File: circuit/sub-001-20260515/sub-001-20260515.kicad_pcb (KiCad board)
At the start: 2 copper layers, 114.3 x 107 mm, 147 parts, among them J1 Conn_NeoPixel, J2 Conn_01x02_Socket, J3 Conn_Power, J4 Conn_Main, Q1 BSS138, Q2 BSS138, Q3 BSS138, Q4 BSS138, Q5 BSS138, Q6 BSS138, Q7 BSS138, Q8 BSS138, U11 LM1117GS-3.3, U12 NE555DR, U13 NE555DR, U14 LM1117GS-3.3, U15 LM1117GS-3.3, U18 NE555DR, U19 NE555DR, U2 LM1117GS-3.3, U20 TSSP58038, U21 TSSP58038, U22 NE555DR, U23 NE555DR, U24 TSSP58038, U25 TSSP58038, U26 HC-SR04, U27 HC-SR04, U28 HC-SR04, U29 HC-SR04, U4 NE555DR, U5 NE555DR, U7 LM1117GS-3.3, U9 LM1117MP-3.3

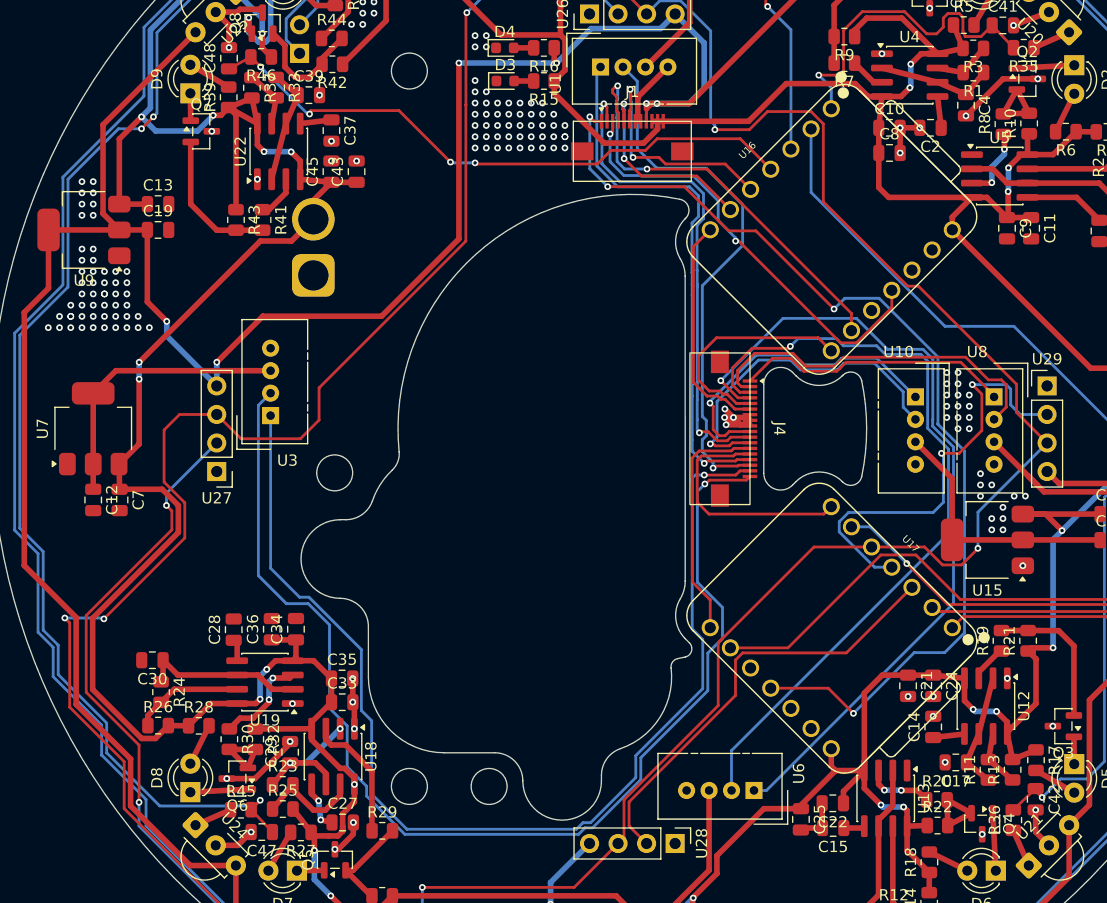
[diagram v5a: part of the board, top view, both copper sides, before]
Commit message: Update ラインセンサ基板の配線を進めた
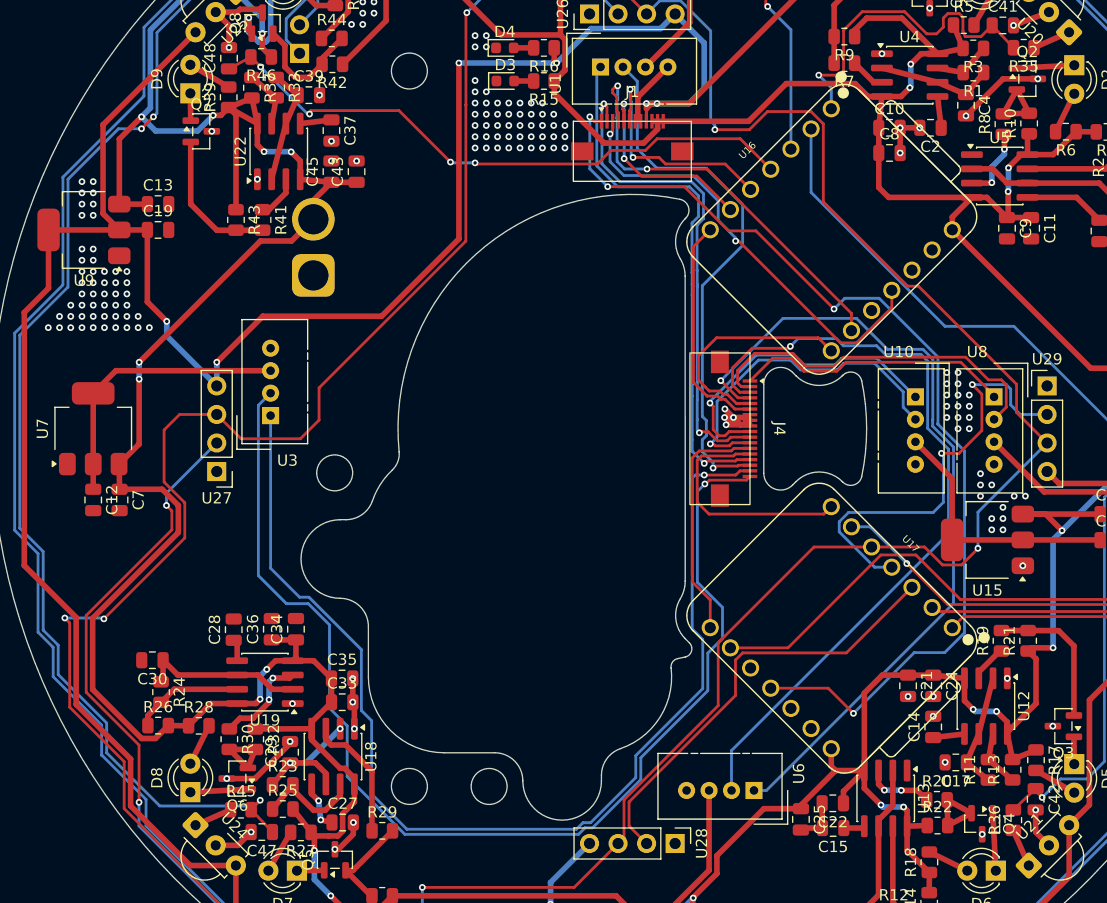
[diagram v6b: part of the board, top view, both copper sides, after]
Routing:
- net 3.3V-unitV4: track 28.3 -> 27.2 mm
- net +5V: track 553.9 -> 553.4 mm, vias 27 -> 26
- net GND: vias 178 -> 175
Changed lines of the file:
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@@
 	)
 	(segment
-		(start 36.04 5)
-		(end 35.285 4.245)
-		(width 0.5)
-		(layer "F.Cu")
-		(net "3.3V-unitV4")
-	)
-	(segment
 		(start 48 -5.39)
 		(end 48 -3.15)
@@
 	)
 	(via
-		(at -50 -10)
-		(size 0.6)
-		(drill 0.3)
-		(layers "F.Cu" "B.Cu")
-		(free yes)
-		(net "GND")
-	)
-	(via
 		(at -25 -36)
 		(size 0.6)
@@
 	)
 	(via
-		(at -6 -26)
-		(size 0.6)
-		(drill 0.3)
-		(layers "F.Cu" "B.Cu")
-		(free yes)
-		(net "GND")
-	)
-	(via
 		(at -48 -21)
 		(size 0.6)
@@
 	)
 	(via
-		(at -47 -12)
-		(size 0.6)
-		(drill 0.3)
-		(layers "F.Cu" "B.Cu")
-		(free yes)
-		(net "GND")
-	)
-	(via
 		(at -14 -31)
 		(size 0.6)
@@
 	)
 	(segment
-		(start 2.25 -26.675)
-		(end 2.25 -27.375)
-		(width 0.5)
-		(layer "F.Cu")
-		(net "+5V")
-	)
-	(segment
 		(start -25.612316 30.24)
 		(end -24.745 31.107316)
@@
 	)
 	(segment
-		(start -2.505 -25.43)
-		(end 1.005 -25.43)
-		(width 0.5)
-		(layer "F.Cu")
-		(net "+5V")
-	)
-	(segment
 		(start 33.36 -18.8)
 		(end 35.51 -18.8)
@@
 	)
 	(segment
+		(start -6.9575 -29.8825)
+		(end -2.505 -25.43)
+		(width 0.5)
+		(layer "F.Cu")
+		(net "+5V")
+	)
+	(segment
+		(start -6.9575 -30.96)
+		(end -6.9575 -29.8825)
+		(width 0.5)
+		(layer "F.Cu")
+		(net "+5V")
+	)
+	(segment
 		(start -27.6725 -34.75)
 		(end -27.668122 -34.75)
@@
 	)
 	(segment
+		(start 2.25 -26.675)
+		(end 2.25 -27.375)
+		(width 0.5)
+		(layer "F.Cu")
+		(net "+5V")
+	)
+	(segment
 		(start 19.7925 -34.92)
 		(end 19.7925 -35.4825)
@@
 	)
 	(segment
-		(start -6.9575 -29.8825)
-		(end -2.505 -25.43)
-		(width 0.5)
-		(layer "F.Cu")
-		(net "+5V")
-	)
-	(segment
 		(start -48.05 16.87)
 		(end -40.42 9.24)
@@
 	)
 	(segment
-		(start -25.79 35.831878)
-		(end -25.79 35.36)
+		(start -5.995 -31.9225)
+		(end -6.9575 -30.96)
 		(width 0.5)
 		(layer "F.Cu")
@@
 	)
 	(segment
-		(start -6.9575 -30.96)
-		(end -5.995 -31.9225)
+		(start -2.505 -25.43)
+		(end 1.005 -25.43)
 		(width 0.5)
 		(layer "F.Cu")
@@
 	)
 	(segment
-		(start -6.9575 -30.96)
-		(end -6.9575 -29.8825)
-		(width 0.5)
-		(layer "F.Cu")
-		(net "+5V")
-	)
-	(segment
 		(start 2.75 -27.375)
 		(end 1.85 -27.375)
@@
 	)
 	(segment
-		(start 1.005 -25.43)
-		(end 2.25 -26.675)
-		(width 0.5)
-		(layer "F.Cu")
-		(net "+5V")
-	)
-	(segment
 		(start 21.945 -21.475)
 		(end 21.945 -24.5525)
@@
 	)
 	(segment
+		(start 1.005 -25.43)
+		(end 2.25 -26.675)
+		(width 0.5)
+		(layer "F.Cu")
+		(net "+5V")
+	)
+	(segment
 		(start 23.9275 -29.5775)
 		(end 22.225 -29.5775)
@@
 	)
 	(via
-		(at -24.745 31.665)
-		(size 0.6)
-		(drill 0.3)
-		(layers "F.Cu" "B.Cu")
-		(net "+5V")
-	)
-	(via
 		(at -26.21 -46.17)
 		(size 0.6)
@@
 	)
 	(segment
-		(start 26.756802 -6.193198)
-		(end 26.535 -6.415)
-		(width 0.25)
-		(layer "B.Cu")
-		(net "RX_{teensy}-TX_{unitV3}")
-	)
-	(segment
 		(start 28.6 1.85)
 		(end 28.6 1.633604)
@@
 	)
 	(segment
-		(start -25.39 30.1)
-		(end -23.66 31.83)
-		(width 0.25)
-		(layer "B.Cu")
-		(net "TX_{teensy}-RX_{unitV2}")
-	)
-	(segment
-		(start -33.2945 -2.0805)
-		(end -33.2945 13.0755)
-		(width 0.25)
-		(layer "B.Cu")
-		(net "TX_{teensy}-RX_{unitV2}")
-	)
-	(segment
-		(start 5.793944 13.657739)
-		(end 5.793944 5.582916)
+		(start -26.958198 17.468198)
+		(end -26.958198 24.887918)
 		(width 0.25)
 		(layer "B.Cu")
@@
 	)
 	(segment
-		(start 5.783236 13.668447)
-		(end 5.793944 13.657739)
+		(start -3.533604 35.53)
+		(end 0.76 31.236396)
 		(width 0.25)
 		(layer "B.Cu")
@@
 	)
 	(segment
-		(start -28.848198 15.578198)
-		(end -26.958198 17.468198)
+		(start -20.256396 36.11)
+		(end -4.783604 36.11)
 		(width 0.25)
 		(layer "B.Cu")
@@
 	)
 	(segment
-		(start -4.783604 36.11)
-		(end -4.203604 35.53)
+		(start 5.793944 13.657739)
+		(end 5.793944 5.582916)
 		(width 0.25)
 		(layer "B.Cu")
@@
 	)
 	(segment
-		(start 8.024485 18.675515)
-		(end 8.024485 15.909696)
+		(start 5.793944 5.582916)
+		(end 6.458778 4.918082)
 		(width 0.25)
 		(layer "B.Cu")
@@
 	)
 	(segment
-		(start -3.533604 35.53)
-		(end 0.76 31.236396)
+		(start -25.39 30.976396)
+		(end -20.256396 36.11)
 		(width 0.25)
 		(layer "B.Cu")
@@
 	)
 	(segment
-		(start -26.958198 24.887918)
-		(end -25.39 26.456116)
+		(start 6.72 23.326396)
+		(end 6.72 19.98)
 		(width 0.25)
 		(layer "B.Cu")
@@
 	)
 	(segment
-		(start -23.66 32.706396)
-		(end -20.256396 36.11)
+		(start -28.848198 15.578198)
+		(end -26.958198 17.468198)
 		(width 0.25)
 		(layer "B.Cu")
@@
 	)
 	(segment
-		(start 0.76 31.236396)
-		(end 0.76 29.286396)
+		(start -25.39 26.456116)
+		(end -25.39 30.976396)
 		(width 0.25)
 		(layer "B.Cu")
@@
 	)
 	(segment
-		(start -33.2945 13.0755)
-		(end -30.791802 15.578198)
+		(start -4.783604 36.11)
+		(end -4.203604 35.53)
 		(width 0.25)
 		(layer "B.Cu")
@@
 	)
 	(segment
-		(start 5.793944 5.582916)
-		(end 6.458778 4.918082)
+		(start 8.024485 15.909696)
+		(end 5.783236 13.668447)
 		(width 0.25)
 		(layer "B.Cu")
@@
 	)
 	(segment
-		(start -30.791802 15.578198)
-		(end -28.848198 15.578198)
+		(start 0.76 29.286396)
+		(end 6.72 23.326396)
 		(width 0.25)
 		(layer "B.Cu")
@@
 	)
 	(segment
-		(start -23.66 31.83)
-		(end -23.66 32.706396)
+		(start -33.2945 -2.0805)
+		(end -33.2945 13.0755)
 		(width 0.25)
 		(layer "B.Cu")
@@
 	)
 	(segment
-		(start -26.958198 17.468198)
-		(end -26.958198 24.887918)
+		(start -26.958198 24.887918)
+		(end -25.39 26.456116)
 		(width 0.25)
 		(layer "B.Cu")
@@
 	)
 	(segment
-		(start 6.72 19.98)
-		(end 8.024485 18.675515)
+		(start -32.2075 -3.1675)
+		(end -33.2945 -2.0805)
 		(width 0.25)
 		(layer "B.Cu")
@@
 	)
 	(segment
-		(start 8.024485 15.909696)
-		(end 5.783236 13.668447)
+		(start 8.024485 18.675515)
+		(end 8.024485 15.909696)
 		(width 0.25)
 		(layer "B.Cu")
@@
 	)
 	(segment
-		(start 6.72 23.326396)
-		(end 6.72 19.98)
+		(start -4.203604 35.53)
+		(end -3.533604 35.53)
 		(width 0.25)
 		(layer "B.Cu")
@@
 	)
 	(segment
-		(start -25.39 26.456116)
-		(end -25.39 30.1)
+		(start 6.72 19.98)
+		(end 8.024485 18.675515)
 		(width 0.25)
 		(layer "B.Cu")
@@
 	)
 	(segment
-		(start -20.256396 36.11)
-		(end -4.783604 36.11)
+		(start -30.791802 15.578198)
+		(end -28.848198 15.578198)
 		(width 0.25)
 		(layer "B.Cu")
@@
 	)
 	(segment
-		(start -32.2075 -3.1675)
-		(end -33.2945 -2.0805)
+		(start 5.783236 13.668447)
+		(end 5.793944 13.657739)
 		(width 0.25)
 		(layer "B.Cu")
@@
 	)
 	(segment
-		(start 0.76 29.286396)
-		(end 6.72 23.326396)
+		(start 0.76 31.236396)
+		(end 0.76 29.286396)
 		(width 0.25)
 		(layer "B.Cu")
@@
 	)
 	(segment
-		(start -4.203604 35.53)
-		(end -3.533604 35.53)
+		(start -33.2945 13.0755)
+		(end -30.791802 15.578198)
 		(width 0.25)
 		(layer "B.Cu")

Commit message: Update サブ基板完成した、再DRおなしゃあす
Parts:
- moved U15 1.05 mm to (30.6, 9.90)
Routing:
- net 3.3V-unitV5: track 23.3 -> 27.5 mm
- net +3.3V: track 397.5 -> 400.1 mm
- net 3.3V-unitV4: track 27.2 -> 29.1 mm
- net 3.3V-unitV1: track 26.8 -> 28.3 mm
- net 3.3V-unitV3: track 27.1 -> 28.3 mm
- net +5V: track 553.4 -> 552.5 mm
- net USS_{EN}: track 308.5 -> 309.2 mm
- net 3.3V-unitV2: track 25.2 -> 25.7 mm
- net GND: vias 175 -> 167

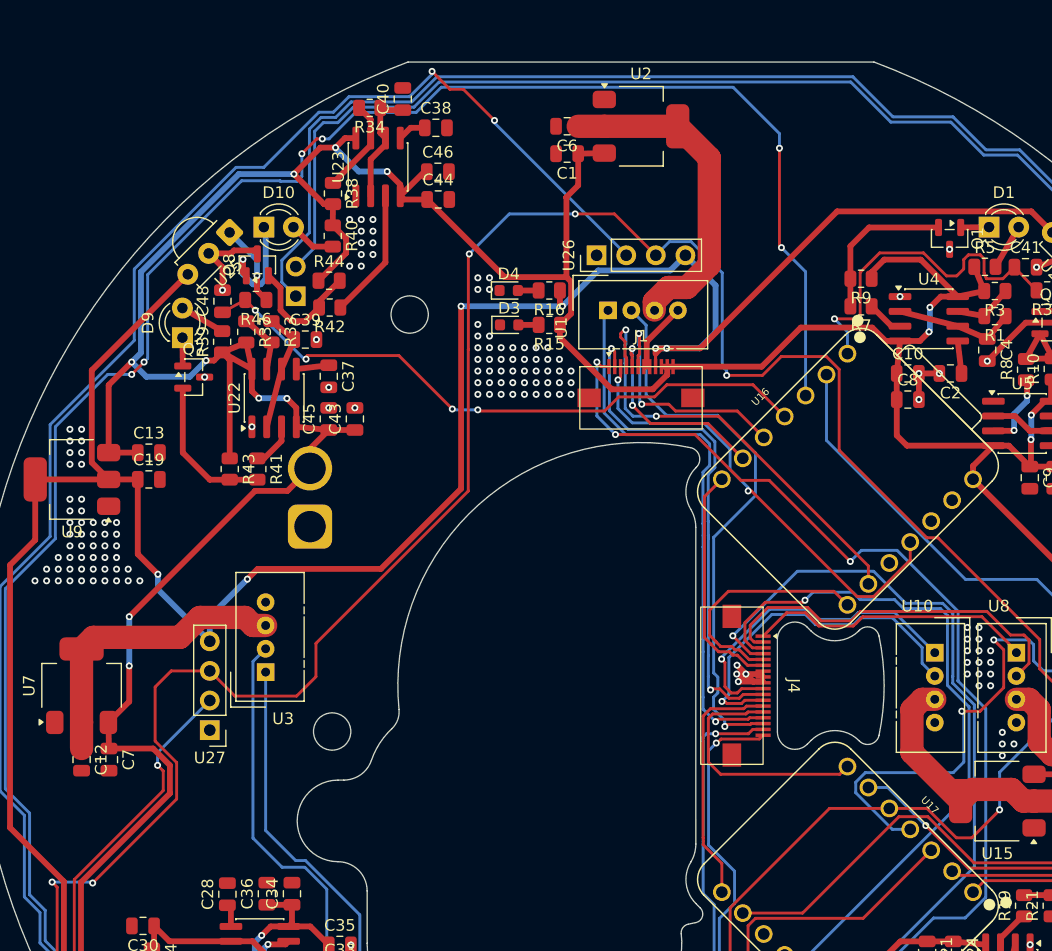
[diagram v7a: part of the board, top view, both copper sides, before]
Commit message: Update サブ基板のDRをした、よさそう
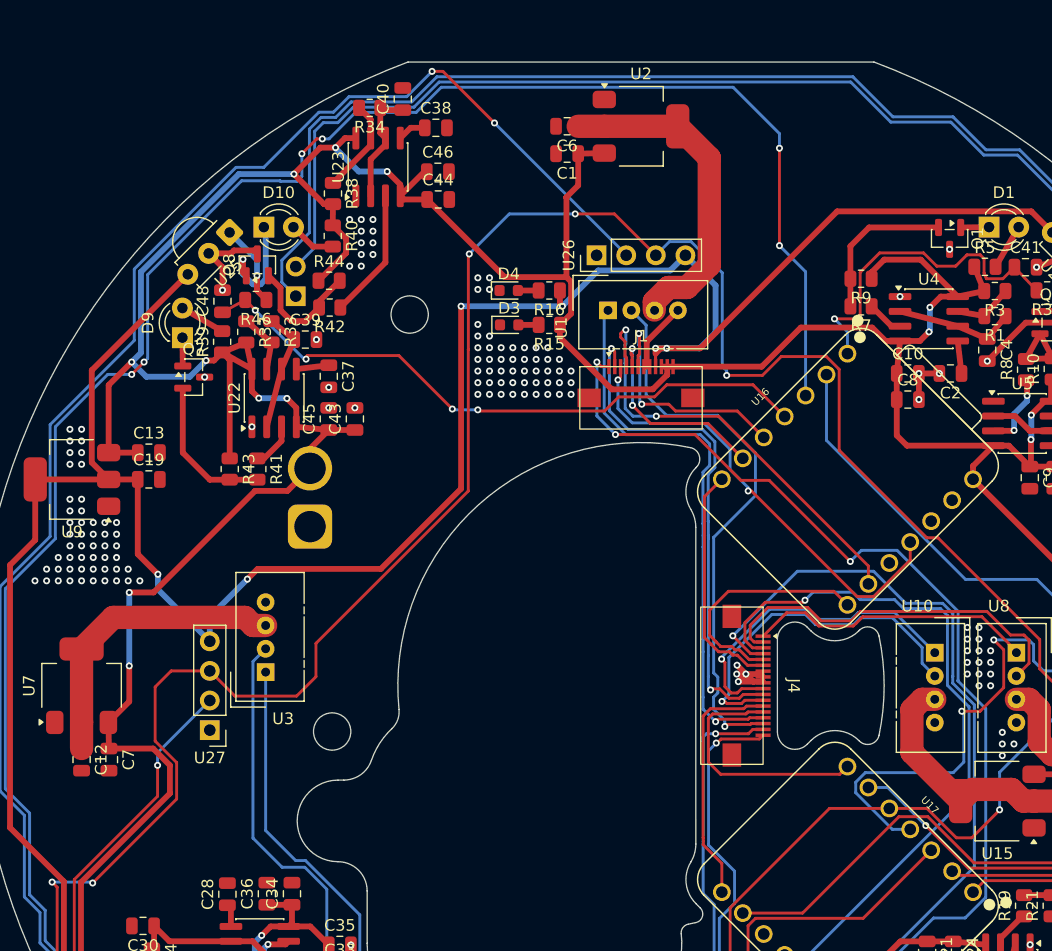
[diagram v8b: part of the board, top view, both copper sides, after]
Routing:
- net +5V: track 552.5 -> 553.7 mm
- net IR_sig1: track 30.3 -> 29.1 mm
